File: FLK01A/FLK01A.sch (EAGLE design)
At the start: 29 parts, among them J1 M10SMD_MALE, J2 M10SMD_MALE, U1 LPC812TSSOP20, U2 EKMBTO5, U3 HTU21DSMD, U4 MMA8452Q, U5 VCNL4000, U6 MPL3115A2LGA8, Y1 12MHZ

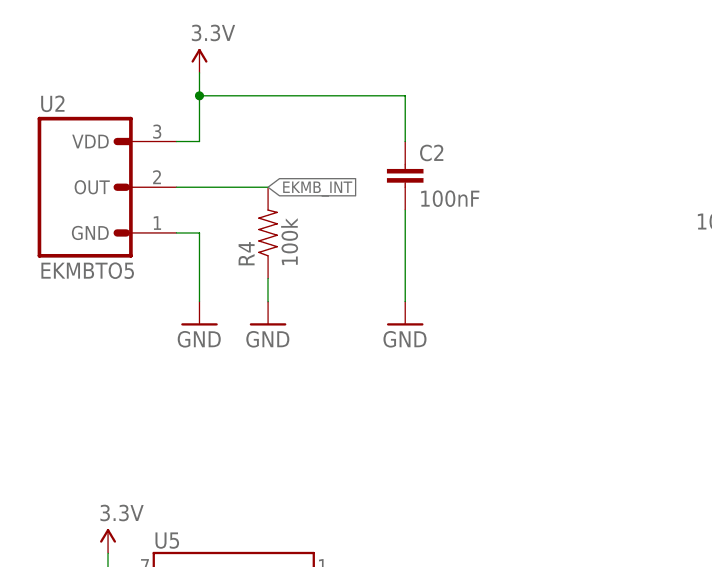
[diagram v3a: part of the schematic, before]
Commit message: [pcb] correct HTU21D footprint
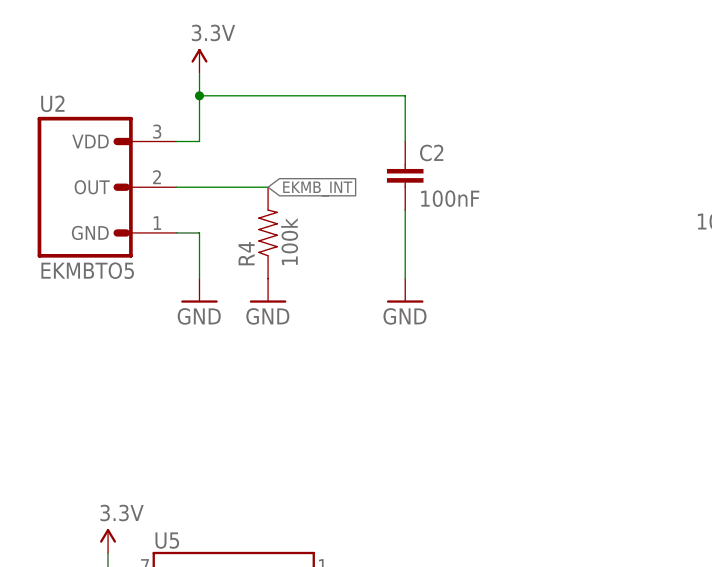
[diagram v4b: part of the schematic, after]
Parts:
- U3: device flukso:HTU21DSMD -> SparkFun-Sensors:HTU21DSMD
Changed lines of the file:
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@@
 <layer number="108" name="tplace-old" color="10" fill="1" visible="yes" active="yes"/>
 <layer number="109" name="ref-old" color="11" fill="1" visible="yes" active="yes"/>
+<layer number="110" name="fp0" color="7" fill="1" visible="yes" active="yes"/>
+<layer number="111" name="LPC17xx" color="7" fill="1" visible="yes" active="yes"/>
+<layer number="112" name="tSilk" color="7" fill="1" visible="yes" active="yes"/>
+<layer number="113" name="IDFDebug" color="7" fill="1" visible="yes" active="yes"/>
 <layer number="116" name="Patch_BOT" color="9" fill="4" visible="yes" active="yes"/>
 <layer number="121" name="_tsilk" color="7" fill="1" visible="yes" active="yes"/>
 <layer number="122" name="_bsilk" color="7" fill="1" visible="yes" active="yes"/>
+<layer number="123" name="tTestmark" color="7" fill="1" visible="yes" active="yes"/>
+<layer number="124" name="bTestmark" color="7" fill="1" visible="yes" active="yes"/>
 <layer number="125" name="_tNames" color="7" fill="1" visible="no" active="yes"/>
+<layer number="126" name="_bNames" color="7" fill="1" visible="yes" active="yes"/>
+<layer number="127" name="_tValues" color="7" fill="1" visible="yes" active="yes"/>
+<layer number="128" name="_bValues" color="7" fill="1" visible="yes" active="yes"/>
 <layer number="131" name="prix" color="7" fill="1" visible="yes" active="yes"/>
 <layer number="132" name="test" color="7" fill="1" visible="yes" active="yes"/>
 <layer number="144" name="Drill_legend" color="7" fill="1" visible="no" active="yes"/>
 <layer number="151" name="HeatSink" color="7" fill="1" visible="yes" active="yes"/>
+<layer number="152" name="_bDocu" color="7" fill="1" visible="yes" active="yes"/>
 <layer number="199" name="Contour" color="7" fill="1" visible="yes" active="yes"/>
 <layer number="200" name="200bmp" color="1" fill="10" visible="no" active="no"/>
@@
 <layer number="223" name="223bmp" color="24" fill="1" visible="no" active="no"/>
 <layer number="224" name="224bmp" color="25" fill="1" visible="no" active="no"/>
+<layer number="248" name="Housing" color="7" fill="1" visible="yes" active="yes"/>
+<layer number="249" name="Edge" color="7" fill="1" visible="yes" active="yes"/>
 <layer number="250" name="Descript" color="3" fill="1" visible="no" active="no"/>
 <layer number="251" name="SMDround" color="12" fill="11" visible="no" active="no"/>
@@
 <part name="GND15" library="SparkFun-Aesthetics" deviceset="GND" device=""/>
 <part name="GND16" library="SparkFun-Aesthetics" deviceset="GND" device=""/>
-<part name="U3" library="flukso" deviceset="HTU21D" device="SMD"/>
 <part name="D1" library="SparkFun-LED" deviceset="LED-GREEN" device="0603" value="GREEN"/>
 <part name="R9" library="SparkFun-Passives" deviceset="RESISTOR" device="0402-RES" value="1k"/>
@@
 <part name="SUPPLY9" library="SparkFun-Aesthetics" deviceset="3.3V" device=""/>
 <part name="C5" library="flukso" deviceset="CAP" device="0805" value="4.7uF"/>
+<part name="U3" library="SparkFun-Sensors" deviceset="HTU21D" device="SMD"/>
 </parts>
 <sheets>
@@
 <instance part="C1" gate="G$1" x="96.52" y="149.86"/>
 <instance part="GND3" gate="1" x="96.52" y="139.7"/>
-<instance part="GND4" gate="1" x="30.48" y="58.42"/>
+<instance part="GND4" gate="1" x="30.48" y="60.96"/>
 <instance part="SUPPLY3" gate="G$1" x="30.48" y="86.36"/>
 <instance part="C2" gate="G$1" x="53.34" y="73.66"/>
-<instance part="GND5" gate="1" x="53.34" y="58.42"/>
+<instance part="GND5" gate="1" x="53.34" y="60.96"/>
 <instance part="R4" gate="G$1" x="38.1" y="68.58" rot="R90"/>
-<instance part="GND6" gate="1" x="38.1" y="58.42"/>
+<instance part="GND6" gate="1" x="38.1" y="60.96"/>
 <instance part="GND7" gate="1" x="101.6" y="66.04"/>
 <instance part="SUPPLY4" gate="G$1" x="93.98" y="78.74"/>
@@
 <instance part="GND15" gate="1" x="86.36" y="15.24"/>
 <instance part="GND16" gate="1" x="101.6" y="15.24"/>
-<instance part="U3" gate="U$1" x="114.3" y="73.66"/>
 <instance part="D1" gate="G$1" x="248.92" y="127"/>
 <instance part="R9" gate="G$1" x="248.92" y="137.16" rot="R90"/>
@@
 <instance part="SUPPLY9" gate="G$1" x="25.4" y="124.46"/>
 <instance part="C5" gate="G$1" x="170.18" y="71.12" rot="MR0"/>
+<instance part="U3" gate="U$1" x="114.3" y="73.66"/>
 </instances>
 <busses>
@@
 <pinref part="GND4" gate="1" pin="GND"/>
 <wire x1="27.94" y1="68.58" x2="30.48" y2="68.58" width="0.1524" layer="91"/>
-<wire x1="30.48" y1="68.58" x2="30.48" y2="60.96" width="0.1524" layer="91"/>
+<wire x1="30.48" y1="68.58" x2="30.48" y2="63.5" width="0.1524" layer="91"/>
 </segment>
 <segment>
 <pinref part="C2" gate="G$1" pin="2"/>
 <pinref part="GND5" gate="1" pin="GND"/>
-<wire x1="53.34" y1="71.12" x2="53.34" y2="60.96" width="0.1524" layer="91"/>
+<wire x1="53.34" y1="71.12" x2="53.34" y2="63.5" width="0.1524" layer="91"/>
 </segment>
 <segment>
@@
 <pinref part="R4" gate="G$1" pin="1"/>
 <pinref part="GND6" gate="1" pin="GND"/>
-<wire x1="38.1" y1="63.5" x2="38.1" y2="60.96" width="0.1524" layer="91"/>
-</segment>
-<segment>
+</segment>
+<segment>

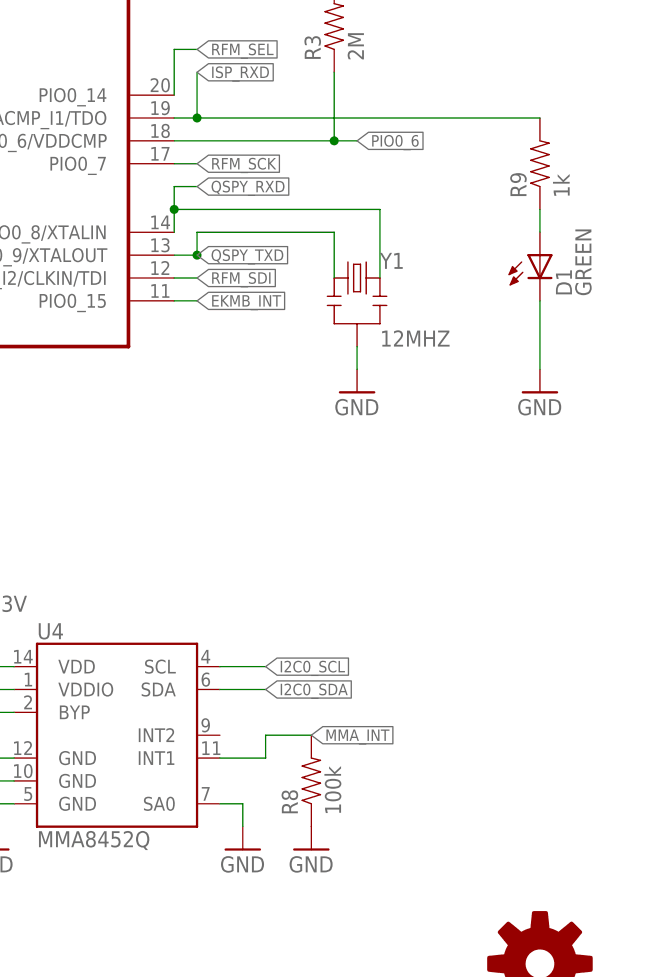
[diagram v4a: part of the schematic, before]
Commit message: [pcb] rename passives
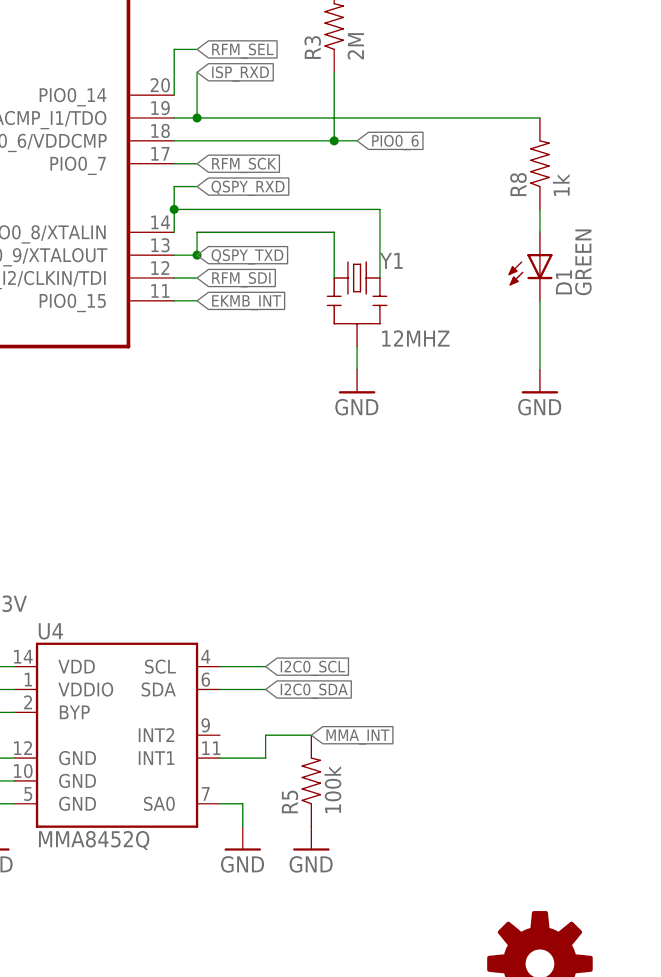
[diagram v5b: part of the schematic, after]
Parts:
- removed R9: 1k, SparkFun-Passives:RESISTOR0402-RES
- added R5: 100k, SparkFun-Passives:RESISTOR0402-RES
- R8: value 100k -> 1k
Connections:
- net GND: now also R5.1; no longer R8.1
- net ISP_RXD: now also R8.2; no longer R9.2
- net MMA_INT: now also R5.2; no longer R8.2
- net N$8: now also R8.1; no longer R9.1
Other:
- moved on the sheet: R8
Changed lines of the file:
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@@
 <part name="C4" library="flukso" deviceset="CAP" device="0402-CAP" value="100nF"/>
 <part name="GND10" library="SparkFun-Aesthetics" deviceset="GND" device=""/>
-<part name="R8" library="SparkFun-Passives" deviceset="RESISTOR" device="0402-RES" value="100k"/>
+<part name="R5" library="SparkFun-Passives" deviceset="RESISTOR" device="0402-RES" value="100k"/>
 <part name="GND11" library="SparkFun-Aesthetics" deviceset="GND" device=""/>
 <part name="U5" library="SparkFun-Sensors" deviceset="VCNL4000" device=""/>
@@
 <part name="GND16" library="SparkFun-Aesthetics" deviceset="GND" device=""/>
 <part name="D1" library="SparkFun-LED" deviceset="LED-GREEN" device="0603" value="GREEN"/>
-<part name="R9" library="SparkFun-Passives" deviceset="RESISTOR" device="0402-RES" value="1k"/>
+<part name="R8" library="SparkFun-Passives" deviceset="RESISTOR" device="0402-RES" value="1k"/>
 <part name="GND17" library="SparkFun-Aesthetics" deviceset="GND" device=""/>
 <part name="J3" library="SparkFun-Connectors" deviceset="M04" device="1X04_NO_SILK"/>
@@
 <instance part="C4" gate="G$1" x="182.88" y="71.12" rot="MR0"/>
 <instance part="GND10" gate="1" x="215.9" y="60.96"/>
-<instance part="R8" gate="G$1" x="223.52" y="68.58" rot="R90"/>
+<instance part="R5" gate="G$1" x="223.52" y="68.58" rot="R90"/>
 <instance part="GND11" gate="1" x="223.52" y="60.96"/>
 <instance part="U5" gate="G$1" x="33.02" y="25.4"/>
@@
 <instance part="GND16" gate="1" x="101.6" y="15.24"/>
 <instance part="D1" gate="G$1" x="248.92" y="127"/>
-<instance part="R9" gate="G$1" x="248.92" y="137.16" rot="R90"/>
+<instance part="R8" gate="G$1" x="248.92" y="137.16" rot="R90"/>
 <instance part="GND17" gate="1" x="248.92" y="111.76"/>
 <instance part="J3" gate="G$1" x="17.78" y="119.38"/>
@@
 </segment>
 <segment>
-<pinref part="R8" gate="G$1" pin="1"/>
+<pinref part="R5" gate="G$1" pin="1"/>
 <pinref part="GND11" gate="1" pin="GND"/>
 </segment>
@@
 <wire x1="213.36" y1="71.12" x2="218.44" y2="71.12" width="0.1524" layer="91"/>
 <wire x1="218.44" y1="71.12" x2="218.44" y2="73.66" width="0.1524" layer="91"/>
-<pinref part="R8" gate="G$1" pin="2"/>
+<pinref part="R5" gate="G$1" pin="2"/>
 <wire x1="218.44" y1="73.66" x2="223.52" y2="73.66" width="0.1524" layer="91"/>
 <label x="223.52" y="73.66" size="1.27" layer="95" xref="yes"/>
@@
 <wire x1="210.82" y1="142.24" x2="210.82" y2="147.32" width="0.1524" layer="91"/>
 <label x="210.82" y="147.32" size="1.27" layer="95" xref="yes"/>
-<pinref part="R9" gate="G$1" pin="2"/>
+<pinref part="R8" gate="G$1" pin="2"/>
 <wire x1="210.82" y1="142.24" x2="248.92" y2="142.24" width="0.1524" layer="91"/>
 <junction x="210.82" y="142.24"/>
@@
 <net name="N$8" class="0">
 <segment>
-<pinref part="R9" gate="G$1" pin="1"/>
+<pinref part="R8" gate="G$1" pin="1"/>
 <pinref part="D1" gate="G$1" pin="A"/>
 <wire x1="248.92" y1="132.08" x2="248.92" y2="129.54" width="0.1524" layer="91"/>

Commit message: [pcb] update board layout
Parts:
- U3: device SparkFun-Sensors:HTU21DSMD -> flukso:HTU21DSMD
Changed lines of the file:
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@@
 <part name="SUPPLY9" library="SparkFun-Aesthetics" deviceset="3.3V" device=""/>
 <part name="C5" library="flukso" deviceset="CAP" device="0805" value="4.7uF"/>
-<part name="U3" library="SparkFun-Sensors" deviceset="HTU21D" device="SMD"/>
+<part name="U3" library="flukso" deviceset="HTU21D" device="SMD"/>
 </parts>
 <sheets>

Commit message: [pcb] use smaller + round pads for I2C header
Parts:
- J3: device SparkFun-Connectors:M041X04_NO_SILK -> flukso:M041X04_NO_SILK
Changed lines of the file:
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@@
 <layer number="54" name="bGND_GNDA" color="1" fill="9" visible="no" active="no"/>
 <layer number="56" name="wert" color="7" fill="1" visible="no" active="no"/>
+<layer number="57" name="tCAD" color="7" fill="1" visible="no" active="no"/>
 <layer number="91" name="Nets" color="2" fill="1" visible="yes" active="yes"/>
 <layer number="92" name="Busses" color="1" fill="1" visible="yes" active="yes"/>
@@
 <layer number="97" name="Info" color="7" fill="1" visible="yes" active="yes"/>
 <layer number="98" name="Guide" color="6" fill="1" visible="yes" active="yes"/>
+<layer number="99" name="SpiceOrder" color="7" fill="1" visible="yes" active="yes"/>
 <layer number="100" name="Muster" color="7" fill="1" visible="no" active="no"/>
 <layer number="101" name="Patch_Top" color="12" fill="4" visible="yes" active="yes"/>
@@
 <layer number="132" name="test" color="7" fill="1" visible="yes" active="yes"/>
 <layer number="144" name="Drill_legend" color="7" fill="1" visible="no" active="yes"/>
+<layer number="150" name="Notes" color="7" fill="1" visible="yes" active="yes"/>
 <layer number="151" name="HeatSink" color="7" fill="1" visible="yes" active="yes"/>
 <layer number="152" name="_bDocu" color="7" fill="1" visible="yes" active="yes"/>
+<layer number="153" name="FabDoc1" color="7" fill="1" visible="yes" active="yes"/>
+<layer number="154" name="FabDoc2" color="7" fill="1" visible="yes" active="yes"/>
+<layer number="155" name="FabDoc3" color="7" fill="1" visible="yes" active="yes"/>
 <layer number="199" name="Contour" color="7" fill="1" visible="yes" active="yes"/>
 <layer number="200" name="200bmp" color="1" fill="10" visible="no" active="no"/>
@@
 <part name="R8" library="SparkFun-Passives" deviceset="RESISTOR" device="0402-RES" value="1k"/>
 <part name="GND17" library="SparkFun-Aesthetics" deviceset="GND" device=""/>
-<part name="J3" library="SparkFun-Connectors" deviceset="M04" device="1X04_NO_SILK"/>
 <part name="GND18" library="SparkFun-Aesthetics" deviceset="GND" device=""/>
 <part name="SUPPLY9" library="SparkFun-Aesthetics" deviceset="3.3V" device=""/>
 <part name="C5" library="flukso" deviceset="CAP" device="0805" value="4.7uF"/>
 <part name="U3" library="flukso" deviceset="HTU21D" device="SMD"/>
+<part name="J3" library="flukso" deviceset="M04" device="1X04_NO_SILK"/>
 </parts>
 <sheets>
@@
 <instance part="R8" gate="G$1" x="248.92" y="137.16" rot="R90"/>
 <instance part="GND17" gate="1" x="248.92" y="111.76"/>
-<instance part="J3" gate="G$1" x="17.78" y="119.38"/>
 <instance part="GND18" gate="1" x="25.4" y="114.3"/>
 <instance part="SUPPLY9" gate="G$1" x="25.4" y="124.46"/>
 <instance part="C5" gate="G$1" x="170.18" y="71.12" rot="MR0"/>
 <instance part="U3" gate="U$1" x="114.3" y="73.66"/>
+<instance part="J3" gate="G$1" x="17.78" y="119.38"/>
 </instances>
 <busses>
@@
 </segment>
 <segment>
-<pinref part="J3" gate="G$1" pin="1"/>
 <wire x1="22.86" y1="116.84" x2="25.4" y2="116.84" width="0.1524" layer="91"/>
 <pinref part="GND18" gate="1" pin="GND"/>
+<pinref part="J3" gate="G$1" pin="1"/>
 </segment>
 <segment>
@@
 </segment>
 <segment>
-<pinref part="J3" gate="G$1" pin="2"/>
 <wire x1="22.86" y1="119.38" x2="25.4" y2="119.38" width="0.1524" layer="91"/>
 <label x="25.4" y="119.38" size="1.27" layer="95" xref="yes"/>
+<pinref part="J3" gate="G$1" pin="2"/>
 </segment>
 </net>
@@
 </segment>
 <segment>
-<pinref part="J3" gate="G$1" pin="3"/>
 <wire x1="22.86" y1="121.92" x2="25.4" y2="121.92" width="0.1524" layer="91"/>
 <label x="25.4" y="121.92" size="1.27" layer="95" xref="yes"/>
+<pinref part="J3" gate="G$1" pin="3"/>
 </segment>
 </net>
@@
 </segment>
 <segment>
-<pinref part="J3" gate="G$1" pin="4"/>
 <wire x1="22.86" y1="124.46" x2="25.4" y2="124.46" width="0.1524" layer="91"/>
 <pinref part="SUPPLY9" gate="G$1" pin="3.3V"/>
-</segment>
-</net>
+<pinref part="J3" gate="G$1" pin="4"/>
+</segment>
+</net>

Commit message: [flk/flr] introduce r3 of sensor and radio board
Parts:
- removed J3: (no value), flukso:M041X04_NO_SILK
- added C10: 100nF, flukso:CAP0402-CAP
- C5: device flukso:CAP0805 -> flukso:CAP0805-CAP
- J1, J2: value M10SMD_MALE -> M10SMD_MALE_SHORT; device flukso:M10SMD_MALE -> flukso:M10SMD_MALE_SHORT
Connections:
- removed net N$7: U6.GND
- net 3.3V: no longer J3.4
- net EKMB_INT: now also C10.1
- net GND: now also C10.2, U6.GND; no longer J3.1
- net I2C0_SCL: no longer J3.3
- net I2C0_SDA: no longer J3.2
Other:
- note added: "3"
- note removed: "2"
- moved on the sheet: C2, J2, R4
